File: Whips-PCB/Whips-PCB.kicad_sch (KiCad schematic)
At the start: 28 parts, among them J1 12 VDC, J2 RS422 BUS, J3 SPEAKER 4OHM, J4 TO WHIP, J5 RS422 BUS, SW2 SW_DIP_x06, U2 MAX485ESA+T, U3 SN74AHCT125DR, U4 TSR_1-2450, U5 MAX98357AEWL+T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

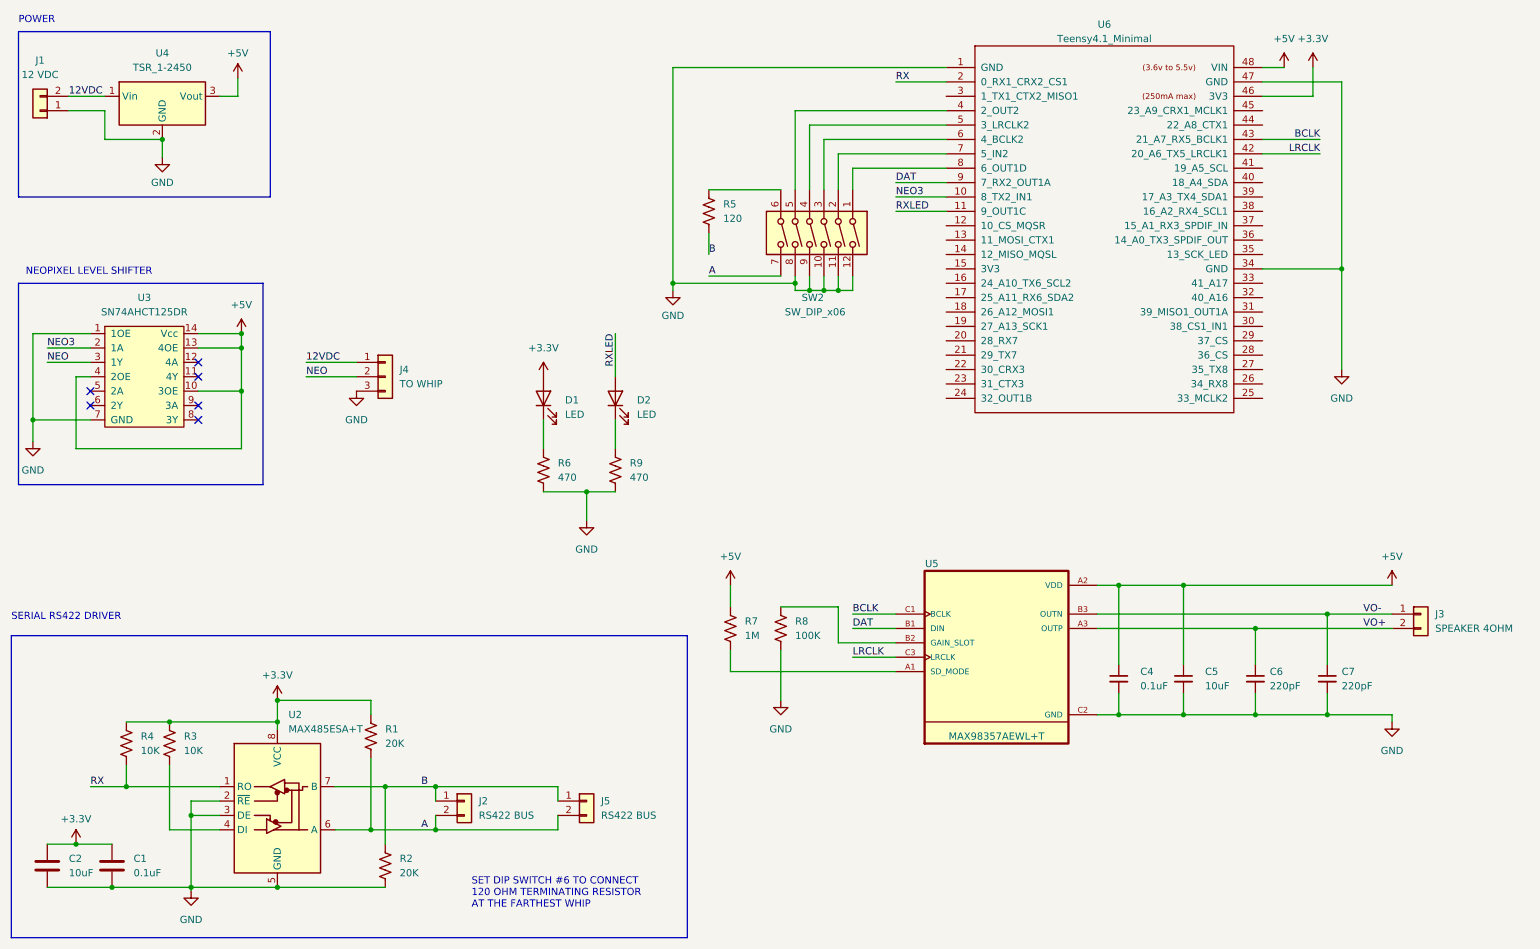
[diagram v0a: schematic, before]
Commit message: full PCB - everything except decorations
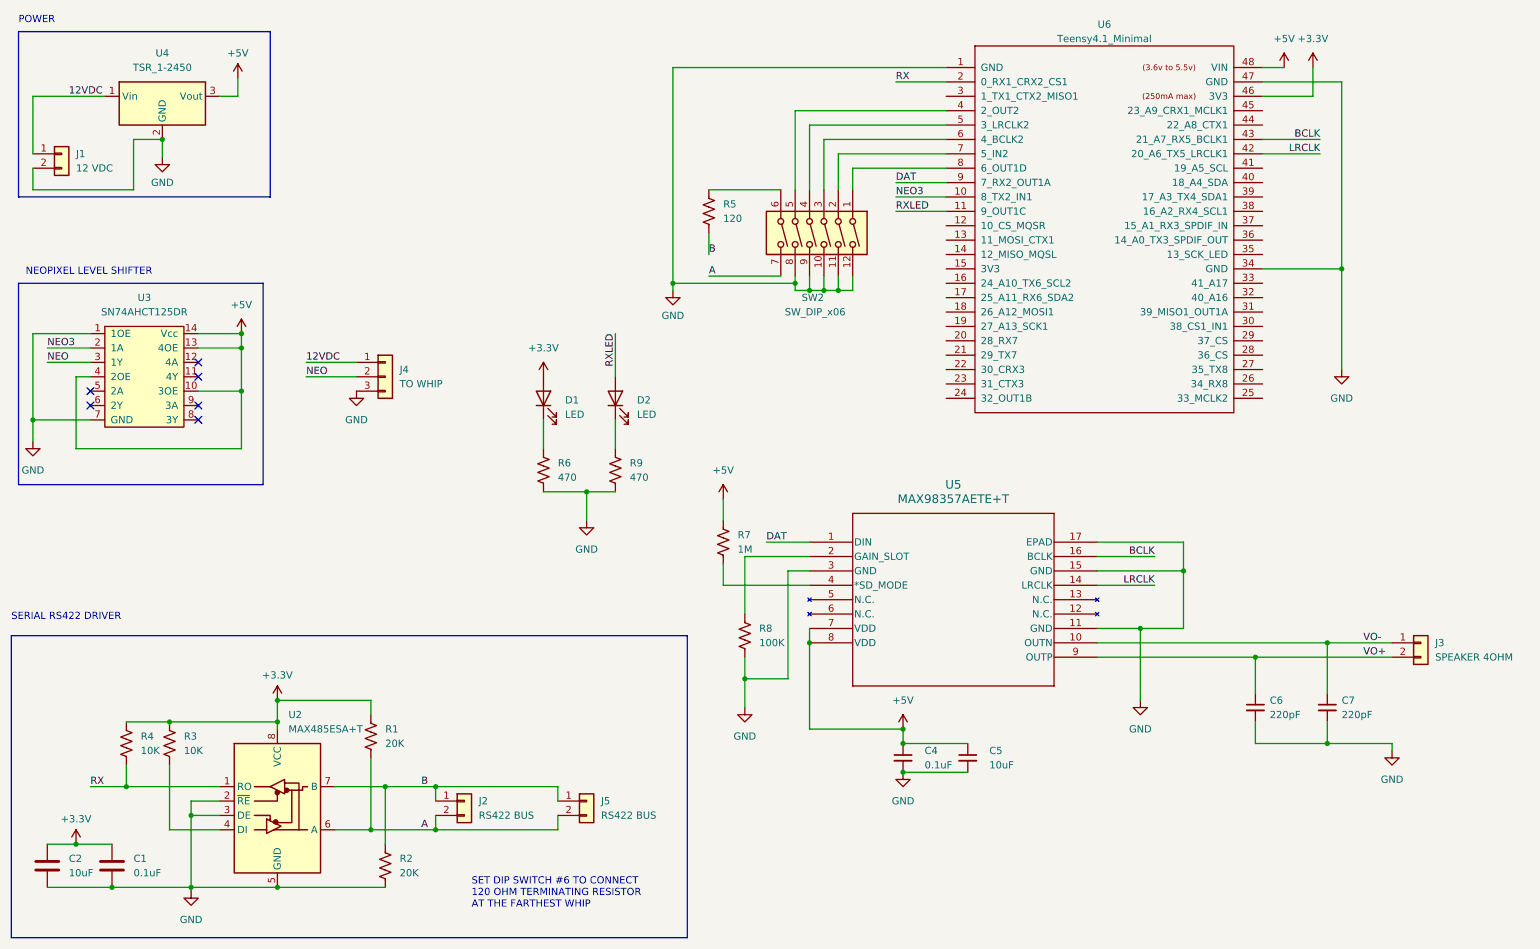
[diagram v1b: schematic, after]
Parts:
- removed U5: MAX98357AEWL+T, Package_BGA:WLP-9_1.448x1.468mm_Layout3x3_P0.4mm_Ball0.27mm_Pad0.25mm, symbol Joels KiCad Symbol Library:MAX98357AEWL_T
- added U5: MAX98357AETE+T, Joels KiCad Footprint Library:MAX98357AETE+T, symbol Joels KiCad Symbol Library:MAX98357AETE+T
- U6: footprint teensy:Teensy41 -> Joels KiCad Footprint Library:Teensy41_Minimal
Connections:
- net +5V: now also U5.7 (VDD), U5.8 (VDD)
- net 12VDC: now also J1.1 (Pin_1); no longer J1.2 (Pin_2)
- net B: now also R2.2; no longer R2.1
- net BCLK: now also U5.16 (BCLK)
- net DAT: now also U5.1 (DIN)
- net GND: now also J1.2 (Pin_2), R2.1, U5.11 (GND), U5.15 (GND), U5.17 (EPAD), U5.3 (GND); no longer J1.1 (Pin_1), R2.2
- net LRCLK: now also U5.14 (LRCLK)
- net VO+: now also U5.9 (OUTP)
- net VO-: now also U5.10 (OUTN)
- net at R8.1: now also U5.2 (GAIN_SLOT)
- net at R7.2: now also U5.4 (*SD_MODE)
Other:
- moved on the sheet: C4, C5, C6, C7, J1, J3, R2, R7, R8

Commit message: cute turtle logo
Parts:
- added H1: DNP (LOGO), Joels KiCad Footprint Library:Turtle-Art-2024, symbol Mechanical:MountingHole
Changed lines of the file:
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@@
+    )
+  )
+  (symbol (lib_id "Mechanical:MountingHole") (at 92.71 41.91 0) (unit 1)
+    (in_bom yes) (on_board yes) (dnp no) (fields_autoplaced)
+    (property "Reference" "H1" (at 95.25 40.64 0)
+      (effects (font (size 1.27 1.27)) (justify left))
+    )
+    (property "Value" "DNP (LOGO)" (at 95.25 43.18 0)
+      (effects (font (size 1.27 1.27)) (justify left))
+    )
+    (property "Footprint" "Joels KiCad Footprint Library:Turtle-Art-2024" (at 92.71 41.91 0)
+      (effects (font (size 1.27 1.27)) hide)
+    )
+    (property "Datasheet" "~" (at 92.71 41.91 0)
+      (effects (font (size 1.27 1.27)) hide)
+    )
+    (instances
+      (project "Whips-PCB"
+        (path "/f51f4695-2f3c-4442-ab83-4885bbbb2720"
+          (reference "H1") (unit 1)
+        )
+      )
     )
   )

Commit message: Much better turtle logo with backlights
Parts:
- added D3, D4: LED, Joels KiCad Footprint Library:Everlight 99-218GLM2C-L7277SGU-TR8-T0-ES side view LED, symbol Device:LED
- added R10, R11: 470, Resistor_SMD:R_0402_1005Metric, symbol Device:R_US
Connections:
- net +3.3V: now also D3.2 (A), D4.2 (A)
- net GND: now also R10.2, R11.2
- new net: D3.1 (K), R10.1
- new net: D4.1 (K), R11.1
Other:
- note added: "side lights for turtle logo"
- moved on the sheet: J4

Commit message: Latest PCBs and some new gitignore stuff
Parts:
- J1, J2, J3, J5: footprint TerminalBlock_RND:TerminalBlock_RND_205-00001_1x02_P5.00mm_Horizontal -> TerminalBlock_Phoenix:TerminalBlock_Phoenix_MKDS-1,5-2_1x02_P5.00mm_Horizontal
- J4: footprint TerminalBlock_RND:TerminalBlock_RND_205-00002_1x03_P5.00mm_Horizontal -> TerminalBlock_Phoenix:TerminalBlock_Phoenix_MKDS-1,5-3_1x03_P5.00mm_Horizontal
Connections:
- no-connect marks 6 -> 38
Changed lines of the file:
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@@
   (junction (at 157.48 71.12) (diameter 0) (color 0 0 0 0)
   )
+  (no_connect (at 237.49 77.47))
+  (no_connect (at 237.49 62.23))
+  (no_connect (at 237.49 82.55))
+  (no_connect (at 237.49 52.07))
+  (no_connect (at 181.61 72.39))
+  (no_connect (at 181.61 62.23))
+  (no_connect (at 237.49 80.01))
+  (no_connect (at 237.49 57.15))
+  (no_connect (at 237.49 87.63))
+  (no_connect (at 181.61 69.85))
+  (no_connect (at 181.61 90.17))
+  (no_connect (at 181.61 85.09))
   (no_connect (at 49.53 91.44))
+  (no_connect (at 181.61 80.01))
+  (no_connect (at 237.49 49.53))
+  (no_connect (at 237.49 59.69))
+  (no_connect (at 237.49 90.17))
+  (no_connect (at 181.61 64.77))
+  (no_connect (at 181.61 59.69))
+  (no_connect (at 237.49 74.93))
   (no_connect (at 30.48 88.9))
+  (no_connect (at 237.49 41.91))
+  (no_connect (at 181.61 77.47))
   (no_connect (at 49.53 86.36))
   (no_connect (at 49.53 93.98))
+  (no_connect (at 237.49 85.09))
+  (no_connect (at 181.61 82.55))
+  (no_connect (at 237.49 64.77))
+  (no_connect (at 181.61 74.93))
+  (no_connect (at 237.49 39.37))
+  (no_connect (at 237.49 54.61))
   (no_connect (at 49.53 83.82))
+  (no_connect (at 237.49 69.85))
+  (no_connect (at 237.49 72.39))
+  (no_connect (at 181.61 67.31))
+  (no_connect (at 181.61 87.63))
   (no_connect (at 30.48 91.44))
+  (no_connect (at 181.61 36.83))
   (wire (pts (xy 53.34 166.37) (xy 44.45 166.37))
     (stroke (width 0) (type default))
@@
       (effects (font (size 1.27 1.27)) (justify left))
     )
-    (property "Footprint" "TerminalBlock_RND:TerminalBlock_RND_205-00001_1x02_P5.00mm_Horizontal" (at 265.43 133.35 0)
+    (property "Footprint" "TerminalBlock_Phoenix:TerminalBlock_Phoenix_MKDS-1,5-2_1x02_P5.00mm_Horizontal" (at 265.43 133.35 0)
       (effects (font (size 1.27 1.27)) hide)
     )
@@
       (effects (font (size 1.27 1.27)) (justify left))
     )
-    (property "Footprint" "TerminalBlock_RND:TerminalBlock_RND_205-00002_1x03_P5.00mm_Horizontal" (at 85.09 60.96 0)
+    (property "Footprint" "TerminalBlock_Phoenix:TerminalBlock_Phoenix_MKDS-1,5-3_1x03_P5.00mm_Horizontal" (at 85.09 60.96 0)
       (effects (font (size 1.27 1.27)) hide)
     )
@@
       (effects (font (size 1.27 1.27)) (justify left))
     )
-    (property "Footprint" "TerminalBlock_RND:TerminalBlock_RND_205-00001_1x02_P5.00mm_Horizontal" (at 96.52 161.29 0)
+    (property "Footprint" "TerminalBlock_Phoenix:TerminalBlock_Phoenix_MKDS-1,5-2_1x02_P5.00mm_Horizontal" (at 96.52 161.29 0)
       (effects (font (size 1.27 1.27)) hide)
     )
@@
       (effects (font (size 1.27 1.27)) (justify left))
     )
-    (property "Footprint" "TerminalBlock_RND:TerminalBlock_RND_205-00001_1x02_P5.00mm_Horizontal" (at 118.11 161.29 0)
+    (property "Footprint" "TerminalBlock_Phoenix:TerminalBlock_Phoenix_MKDS-1,5-2_1x02_P5.00mm_Horizontal" (at 118.11 161.29 0)
       (effects (font (size 1.27 1.27)) hide)
     )
@@
       (effects (font (size 1.27 1.27)) (justify left))
     )
-    (property "Footprint" "TerminalBlock_RND:TerminalBlock_RND_205-00001_1x02_P5.00mm_Horizontal" (at 25.4 46.99 0)
-      (effects (font (size 1.27 1.27)) hide)
-    )
+    (property "Footprint" "TerminalBlock_Phoenix:TerminalBlock_Phoenix_MKDS-1,5-2_1x02_P5.00mm_Horizontal" (at 25.4 46.99 0)
+      (effects (font (size 1.27 1.27)) hide)
+    )
